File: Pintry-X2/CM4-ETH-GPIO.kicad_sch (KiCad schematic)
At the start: 53 parts, among them J3 JD0-0001NL, J4 DM3D-SF, J5 UART, J6 Expansion, J7 Fan, J8 Fan, Q1 BSS138PW, Q2 BSS138PW, SW1 SW_Push, U3 SN74LVC1G17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

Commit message: Cleaned up schematic
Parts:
- added C? (x2): 10uF, PintryParts-Footprints:C_0402_1005Metric, symbol Device:C_Small
- J6: footprint (none) -> Connector_PinHeader_2.54mm:PinHeader_2x05_P2.54mm_Vertical
- gave numbers to parts that had none: 7
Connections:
- net +3V3: now also J6.2 (Pin_2), C?.1
- net +5V: now also J6.4 (Pin_4), C?.1
- net GND: now also J6.10 (Pin_10), C?.2, C?.2
- net SCL1: now also J6.7 (Pin_7)
- net SDA1: now also J6.9 (Pin_9)
- net GPIO7: now reaches Module1.37 (GPIO7)
- net GPIO7: now also J6.6 (Pin_6)
- net GPIO11: now reaches Module1.38 (GPIO11)
- net GPIO11: now also J6.5 (Pin_5)
- net GPIO8: now reaches Module1.39 (GPIO8)
- net GPIO8: now also J6.8 (Pin_8)
- net GPIO9: now reaches Module1.40 (GPIO9)
- net GPIO9: now also J6.3 (Pin_3)
- net GPIO10: now reaches Module1.44 (GPIO10)
- net GPIO10: now also J6.1 (Pin_1)
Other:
- note added: "Compute Module 4 - Connector A"
- note added: "Gigabit Ethernet"
- note added: "MicroSD Card Holder (Optional for CM4 Lite SoM)"
- note added: "Power button"
- note added: "UART, Expansion and status LEDs"
- note added: "When the CM4 is OFF, pressing the button wakes it up. When the CM4 is ON, pressing the button shuts it down (needs custom Device Tree Overlay)."
- note removed: "MicroUSB (Optional for CM4 Lite SoM)"
- moved on the sheet: C1, C10, C11, C12, C13, C14, C15, C16, C17, C3, C8, C9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

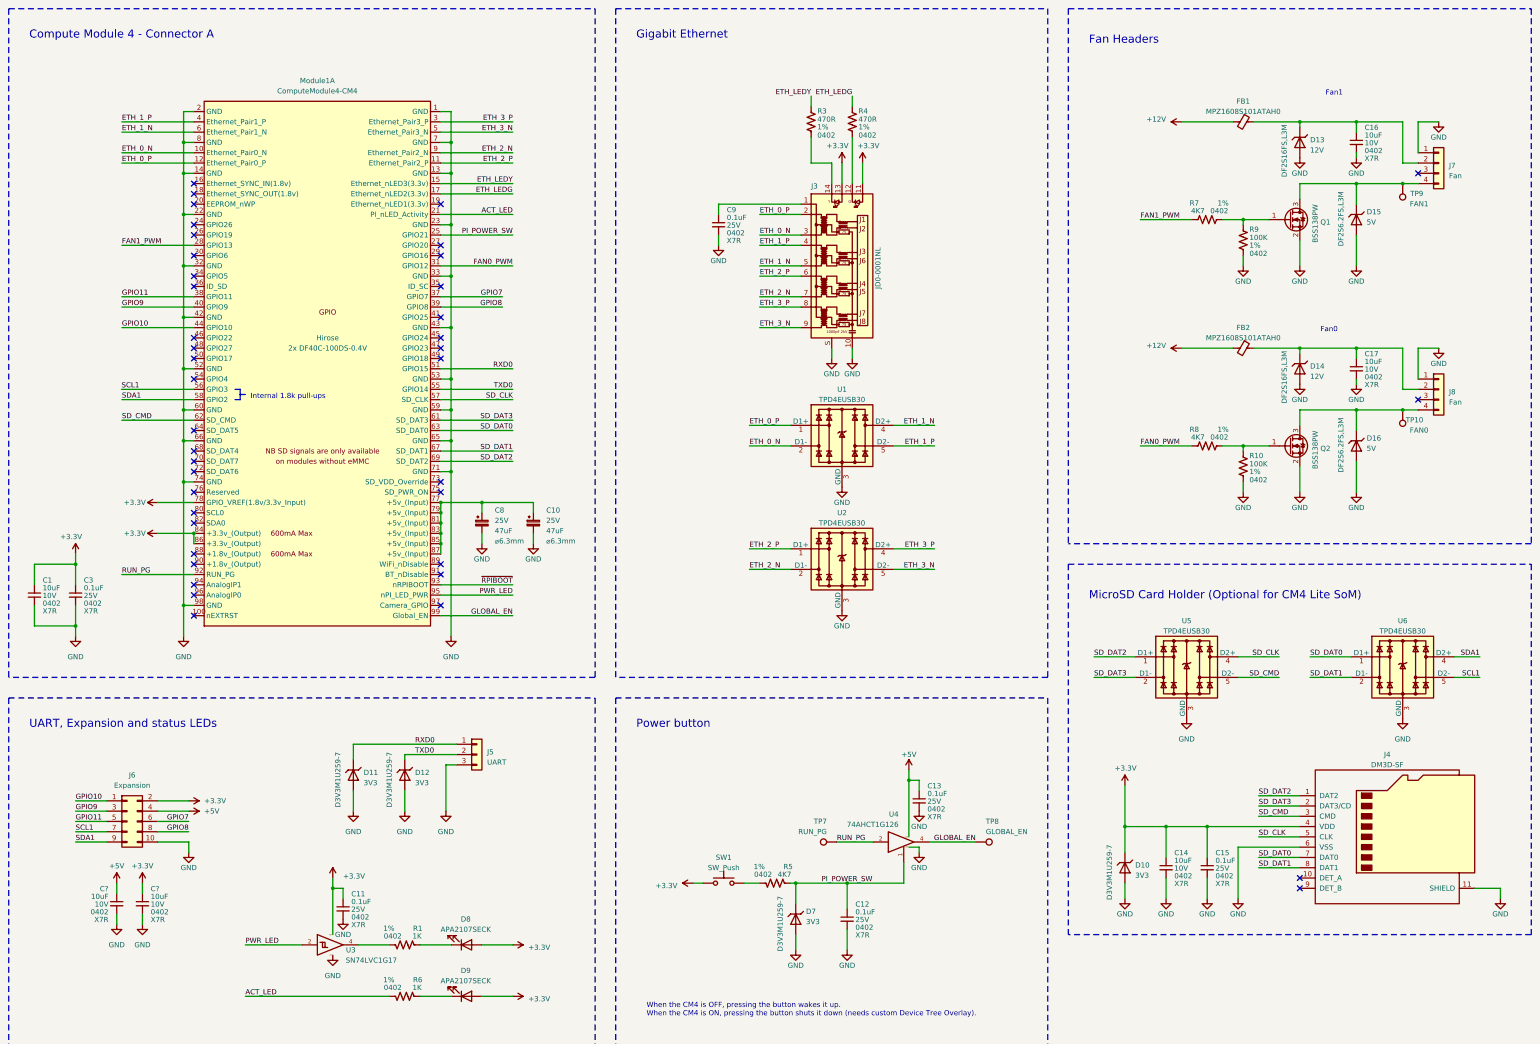
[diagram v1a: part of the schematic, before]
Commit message: Finished Shematic. Starting PCB
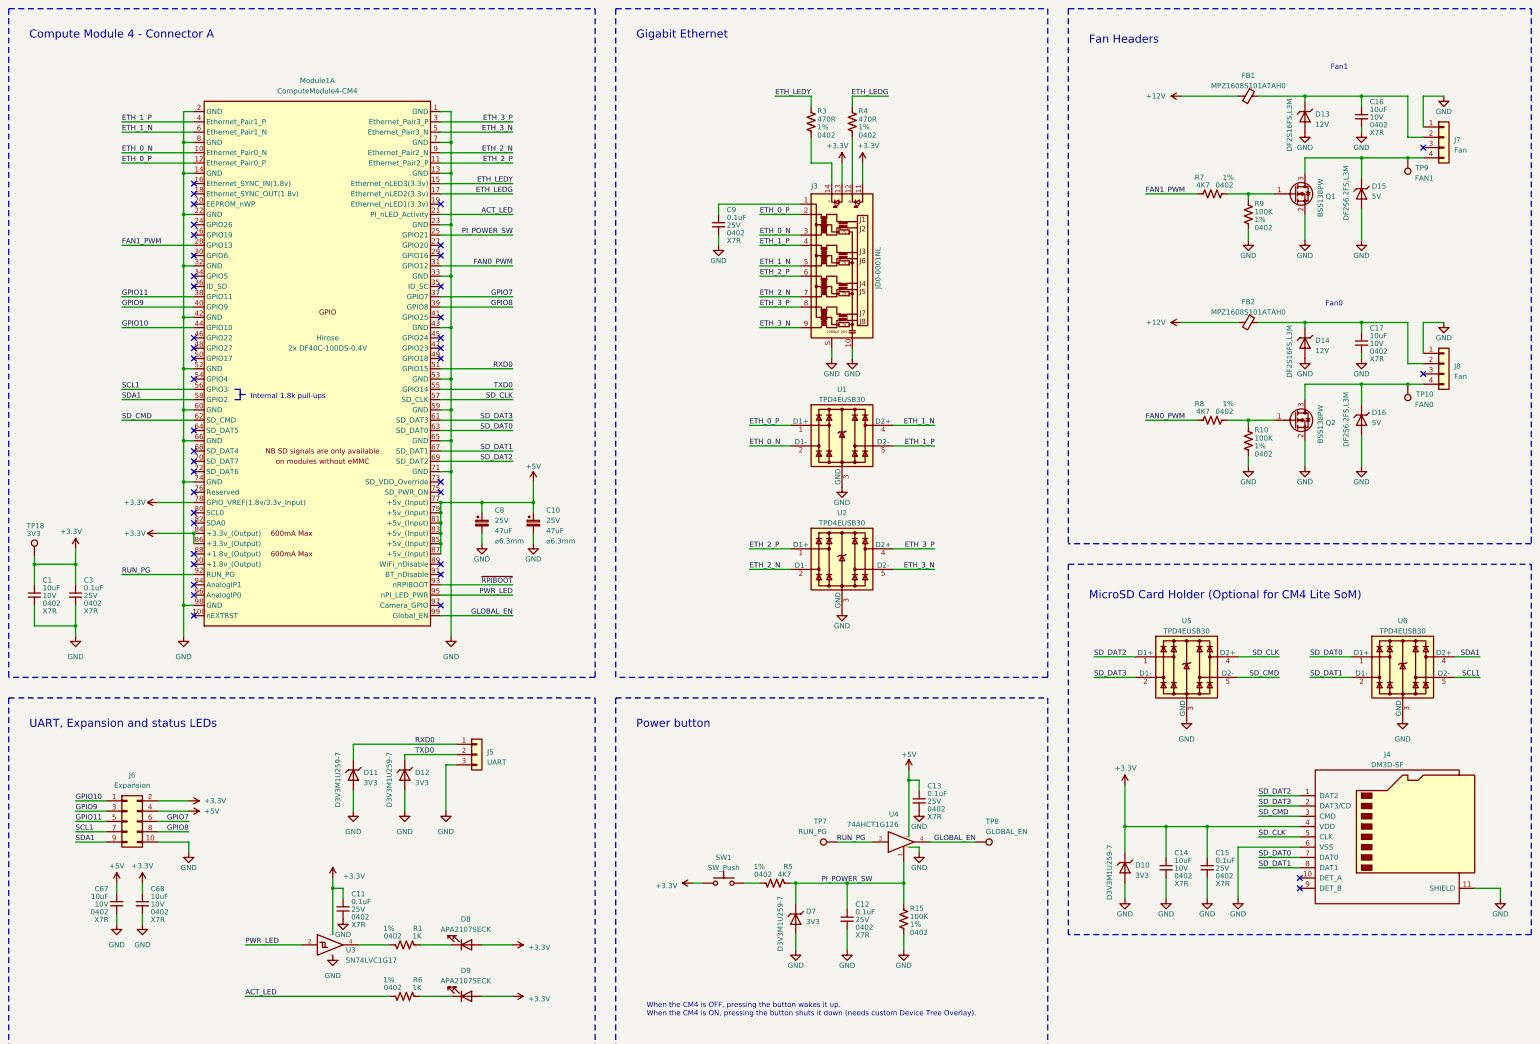
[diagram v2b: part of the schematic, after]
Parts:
- added R15: 100K, PintryParts-Footprints:R_0402_1005Metric, symbol Device:R_US
- added TP18: 3V3, TestPoint:TestPoint_Pad_D1.0mm, symbol Connector:TestPoint
- Module1: footprint CM4IO:Raspberry-Pi-4-Compute-Module -> PintryParts-Footprints:Raspberry-Pi-4-Compute-Module
- TP10, TP7, TP8, TP9: footprint TestPoint:TestPoint_Pad_D2.5mm -> TestPoint:TestPoint_Pad_D1.0mm
- gave numbers to parts that had none: 2
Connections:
- net +3V3: now also TP18.1
- net +5V: now also C10.1, C8.1, Module1.77 (+5v_(Input)), Module1.79 (+5v_(Input)), Module1.81 (+5v_(Input)), Module1.83 (+5v_(Input)), Module1.85 (+5v_(Input)), Module1.87 (+5v_(Input))
- net GND: now also R15.2
- net PI_POWER_SW: now also R15.1
- net SCL1: now also Module1.56 (GPIO3)
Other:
- moved on the sheet: C16, C17, D13, D14, D15, D16, FB1, FB2, J7, J8, Q1, Q2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

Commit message: PCB Routing Complete - needs review
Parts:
- added R19, R20: 1K, PintryParts-Footprints:R_0402_1005Metric, symbol Device:R_US
- TP10, TP18, TP7, TP8, TP9: footprint TestPoint:TestPoint_Pad_D1.0mm -> PintryParts-Footprints:TestPoint_Pad_D1.0mm
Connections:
- net +5V: now also J6.1 (Pin_1); no longer J6.4 (Pin_4)
- net ETH_1_N: now also J3.4; no longer J3.5
- net ETH_1_P: now also J3.5; no longer J3.4
- net GPIO10: now also J6.5 (Pin_5); no longer J6.1 (Pin_1)
- net GPIO11: now also J6.9 (Pin_9); no longer J6.5 (Pin_5)
- net GPIO9: now also J6.7 (Pin_7); no longer J6.3 (Pin_3)
- net RXD0: now also R19.2; no longer J5.1 (Pin_1)
- net SCL1: now also J6.3 (Pin_3); no longer J6.7 (Pin_7), U6.5 (D2-), U6.6
- net SDA1: now also J6.4 (Pin_4); no longer J6.9 (Pin_9), U6.4 (D2+), U6.7
- net SD_CLK: now also U6.4 (D2+), U6.7; no longer U5.4 (D2+), U5.7
- net SD_CMD: now also U5.2 (D1-), U5.9; no longer U5.5 (D2-), U5.6
- net SD_DAT0: now also U6.2 (D1-), U6.9; no longer U6.1 (D1+), U6.10
- net SD_DAT1: now also U6.1 (D1+), U6.10; no longer U6.2 (D1-), U6.9
- net SD_DAT2: now also U5.5 (D2-), U5.6; no longer U5.1 (D1+), U5.10
- net SD_DAT3: now also U5.4 (D2+), U5.7; no longer U5.2 (D1-), U5.9
- net TXD0: now also R20.2; no longer J5.2 (Pin_2)
- net ~RPIBOOT renamed ~{RPIBOOT}
- new net: U6.5 (D2-), U6.6
- new net: J5.1 (Pin_1), R19.1
- new net: J5.2 (Pin_2), R20.1
- new net: U5.1 (D1+), U5.10
- no-connect marks 41 -> 43
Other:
- moved on the sheet: D11, D12

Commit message: Fixed ON/OFF Button
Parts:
- removed D7: D3V3M1U259-7, Diode_SMD:D_SOD-923, symbol PintryParts-Symbols:D3V3M1U259-7
- added D7: DF2S6.2FS,L3M, Diode_SMD:D_SOD-923, symbol PintryParts-Symbols:DF2S6.2FS,L3M
- added R36: 100K, PintryParts-Footprints:R_0402_1005Metric, symbol Device:R_US
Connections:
- net +3V3: no longer SW1.1
- net +5V: now also SW1.1
- net GND: now also D7.2 (A), R36.2; no longer R15.2
- net PI_POWER_SW: now also R15.2, R36.1; no longer C12.1, R15.1, R5.1, U4.1
- new net: C12.1, D7.1 (K), R15.1, R5.1, U4.1
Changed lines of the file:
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@@
   (junction (at 232.41 236.22) (diameter 0.9144) (color 0 0 0 0))
   (junction (at 246.38 236.22) (diameter 0.9144) (color 0 0 0 0))
+  (junction (at 246.38 251.46) (diameter 0) (color 0 0 0 0))
   (junction (at 247.65 210.82) (diameter 0.9144) (color 0 0 0 0))
   (junction (at 300.99 222.25) (diameter 0.9144) (color 0 0 0 0))
@@
     (stroke (width 0) (type solid) (color 0 0 0 0))
   )
-  (wire (pts (xy 246.38 248.92) (xy 246.38 252.73))
-    (stroke (width 0) (type solid) (color 0 0 0 0))
+  (wire (pts (xy 246.38 248.92) (xy 246.38 251.46))
+    (stroke (width 0) (type solid) (color 0 0 0 0))
+  )
+  (wire (pts (xy 246.38 251.46) (xy 246.38 252.73))
+    (stroke (width 0) (type solid) (color 0 0 0 0))
+  )
+  (wire (pts (xy 246.38 251.46) (xy 265.43 251.46))
+    (stroke (width 0) (type default) (color 0 0 0 0))
+  )
+  (wire (pts (xy 246.38 260.35) (xy 246.38 262.89))
+    (stroke (width 0) (type default) (color 0 0 0 0))
   )
   (wire (pts (xy 247.65 208.28) (xy 247.65 210.82))
@@
   )
   (text "When the CM4 is OFF, pressing the button wakes it up.\nWhen the CM4 is ON, pressing the button shuts it down (needs custom Device Tree Overlay)."
-    (at 182.88 269.24 0)
+    (at 182.88 273.05 0)
     (effects (font (size 1.27 1.27)) (justify left bottom))
   )
@@
     (effects (font (size 1.27 1.27)) (justify left bottom))
   )
-  (label "PI_POWER_SW" (at 226.06 236.22 0)
-    (effects (font (size 1.27 1.27)) (justify left bottom))
-  )
   (label "RUN_PG" (at 229.87 226.06 0)
     (effects (font (size 1.27 1.27)) (justify left bottom))
@@
   )
   (label "GLOBAL_EN" (at 264.16 226.06 180)
+    (effects (font (size 1.27 1.27)) (justify right bottom))
+  )
+  (label "PI_POWER_SW" (at 265.43 251.46 180)
     (effects (font (size 1.27 1.27)) (justify right bottom))
   )
@@
     (pin "1")
   )
-  (symbol (lib_id "power:+3.3V") (at 194.31 236.22 90) (unit 1)
-    (in_bom yes) (on_board yes) (fields_autoplaced)
+  (symbol (lib_id "power:+5V") (at 194.31 236.22 90) (unit 1)
+    (in_bom yes) (on_board yes)
     (property "Reference" "#PWR034" (id 0) (at 198.12 236.22 0)
       (effects (font (size 1.27 1.27)) hide)
     )
-    (property "Value" "+3.3V" (id 1) (at 190.5 236.8549 90)
+    (property "Value" "+5V" (id 1) (at 190.5 236.2201 90)
       (effects (font (size 1.27 1.27)) (justify left))
     )
@@
     (pin "1")
   )
-  (symbol (lib_id "power:GND") (at 246.38 252.73 0) (unit 1)
-    (in_bom yes) (on_board yes)
-    (property "Reference" "#PWR075" (id 0) (at 246.38 259.08 0)
-      (effects (font (size 1.27 1.27)) hide)
-    )
-    (property "Value" "GND" (id 1) (at 246.38 256.54 0))
-    (property "Footprint" "" (id 2) (at 246.38 252.73 0)
-      (effects (font (size 1.27 1.27)) hide)
-    )
-    (property "Datasheet" "" (id 3) (at 246.38 252.73 0)
+  (symbol (lib_id "power:GND") (at 246.38 262.89 0) (unit 1)
+    (in_bom yes) (on_board yes) (fields_autoplaced)
+    (property "Reference" "#PWR075" (id 0) (at 246.38 269.24 0)
+      (effects (font (size 1.27 1.27)) hide)
+    )
+    (property "Value" "GND" (id 1) (at 246.38 266.7 0))
+    (property "Footprint" "" (id 2) (at 246.38 262.89 0)
+      (effects (font (size 1.27 1.27)) hide)
+    )
+    (property "Datasheet" "" (id 3) (at 246.38 262.89 0)
       (effects (font (size 1.27 1.27)) hide)
     )
@@
     )
     (property "Size" "0402" (id 5) (at 247.904 248.412 0)
+      (effects (font (size 1.27 1.27)) (justify left))
+    )
+    (pin "1")
+    (pin "2")
+  )
+  (symbol (lib_id "Device:R_US") (at 246.38 256.54 0) (unit 1)
+    (in_bom yes) (on_board yes)
+    (property "Reference" "R36" (id 0) (at 247.904 253.8729 0)
+      (effects (font (size 1.27 1.27)) (justify left))
+    )
+    (property "Value" "100K" (id 1) (at 247.904 255.9049 0)
+      (effects (font (size 1.27 1.27)) (justify left))
+    )
+    (property "Footprint" "PintryParts-Footprints:R_0402_1005Metric" (id 2) (at 247.396 256.794 90)
+      (effects (font (size 1.27 1.27)) hide)
+    )
+    (property "Datasheet" "~" (id 3) (at 246.38 256.54 0)
+      (effects (font (size 1.27 1.27)) hide)
+    )
+    (property "Tolerance" "1%" (id 4) (at 247.904 257.81 0)
+      (effects (font (size 1.27 1.27)) (justify left))
+    )
+    (property "Size" "0402" (id 5) (at 247.904 259.842 0)
       (effects (font (size 1.27 1.27)) (justify left))
     )
@@
     (pin "2")
   )
-  (symbol (lib_id "PintryParts-Symbols:D3V3M1U259-7") (at 219.71 245.11 270) (unit 1)
+  (symbol (lib_id "PintryParts-Symbols:DF2S6.2FS,L3M") (at 219.71 245.11 270) (unit 1)
     (in_bom yes) (on_board yes)
     (property "Reference" "D7" (id 0) (at 222.25 243.2049 90)
       (effects (font (size 1.27 1.27)) (justify left))
     )
-    (property "Value" "D3V3M1U259-7" (id 1) (at 215.9 239.3949 0)
+    (property "Value" "DF2S6.2FS,L3M" (id 1) (at 215.9 238.1249 0)
       (effects (font (size 1.27 1.27)) (justify left))
     )
@@
       (effects (font (size 1.27 1.27)) hide)
     )
-    (property "Datasheet" "https://www.diodes.com/assets/Datasheets/D3V3M1U2S9.pdf" (id 3) (at 219.71 245.11 0)
-      (effects (font (size 1.27 1.27)) hide)
-    )
-    (property "VRWM" "3V3" (id 4) (at 222.25 245.7449 90)
-      (effects (font (size 1.27 1.27)) (justify left))
-    )
-    (property "Part Number" "D3V3M1U2S9-7" (id 5) (at 219.71 245.11 90)
-      (effects (font (size 1.27 1.27)) hide)
-    )
-    (property "Manufacturer" "Diodes" (id 6) (at 219.71 245.11 90)
-      (effects (font (size 1.27 1.27)) hide)
-    )
+    (property "Datasheet" "https://toshiba.semicon-storage.com/info/docget.jsp?did=22218&prodName=DF2S6.2FS" (id 3) (at 219.71 245.11 0)
+      (effects (font (size 1.27 1.27)) hide)
+    )
+    (property "VRWM" "5V" (id 4) (at 222.25 245.7449 90)
+      (effects (font (size 1.27 1.27)) (justify left))
+    )
+    (property "Manufacturer" "Toshiba" (id 5) (at 219.71 245.11 90)
+      (effects (font (size 1.27 1.27)) hide)
+    )
+    (property "Part Number" "DF2S6.2FS,L3M" (id 6) (at 219.71 245.11 90)
+      (effects (font (size 1.27 1.27)) hide)
+    )
